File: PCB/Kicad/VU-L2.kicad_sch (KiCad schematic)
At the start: 32 parts, among them U3 SR1-L2, U4 SR2-L2

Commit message: PDF
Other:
- note added: "VU LINE 2"
- moved on the sheet: D31, D32, D33, D34, D35, D36, D37, D38, D39, D40, D41, D42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

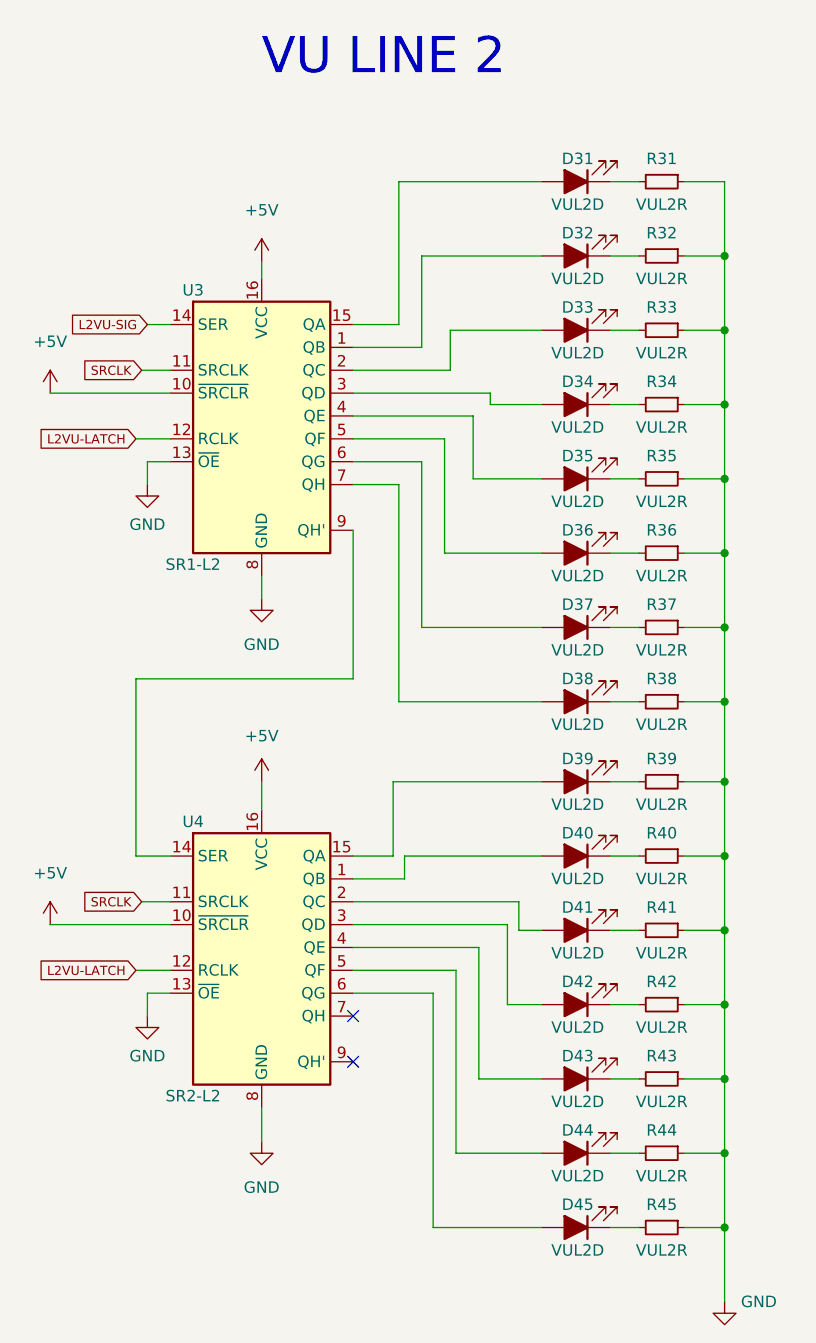
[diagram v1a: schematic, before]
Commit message: added transistor and 3x leds play- cue
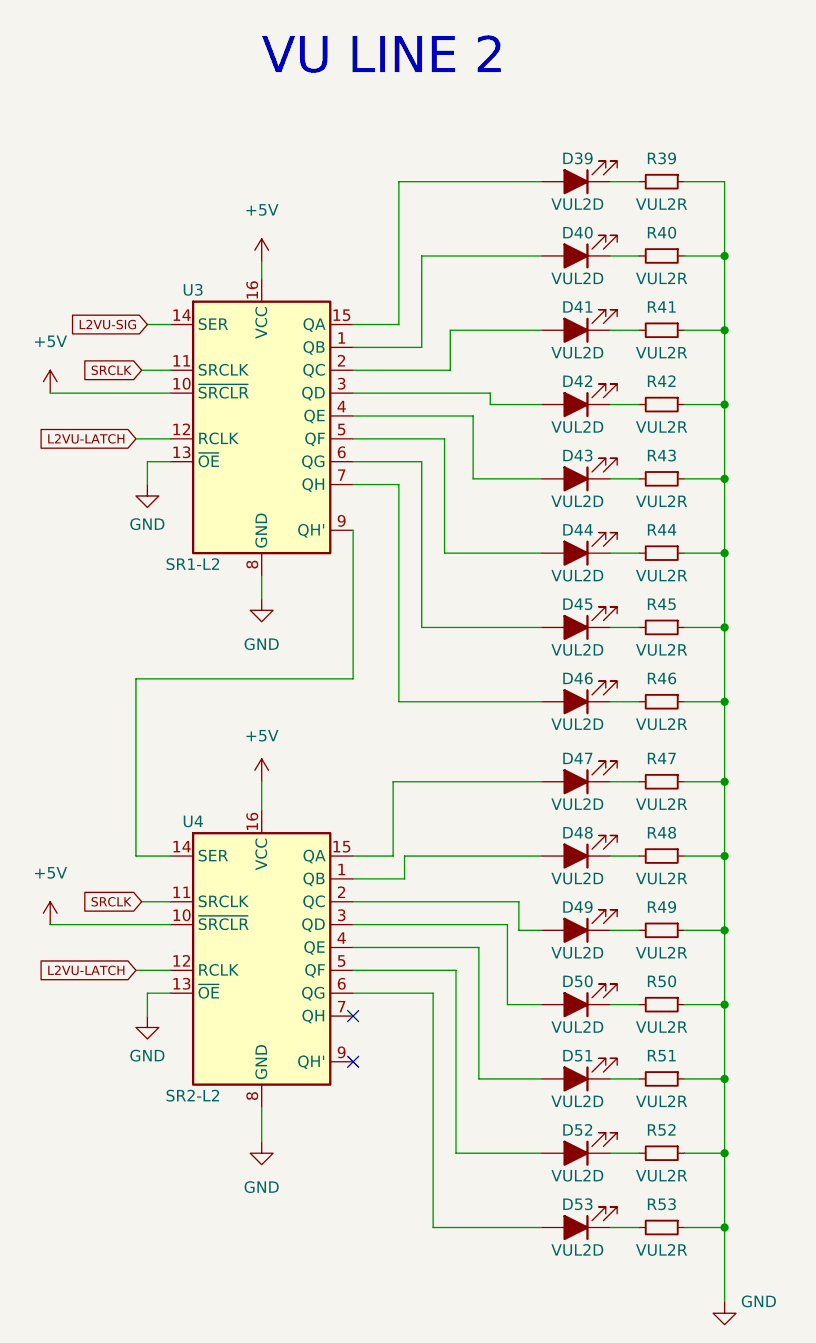
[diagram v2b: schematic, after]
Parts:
- U3, U4: footprint (none) -> Library:SO-16_3.9x9.9mm_P1.27mm
- renumbered D31 to D39, D32 to D40, D33 to D41, D34 to D42, D35 to D43, D36 to D44, D37 to D45, D38 to D46, D39 to D47, D40 to D48, D41 to D49, D42 to D50, D43 to D51, D44 to D52, D45 to D53, R31 to R39, R32 to R40, R33 to R41, R34 to R42, R35 to R43, R36 to R44, R37 to R45, R38 to R46, R39 to R47, R40 to R48, R41 to R49, R42 to R50, R43 to R51, R44 to R52, R45 to R53

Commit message: routing WIP
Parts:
- D48, D49, D50, D51: footprint Library:LED_GREEN -> Library:LED_YELLOW
- D52, D53: footprint Library:LED_GREEN -> Library:LED_RED
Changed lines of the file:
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@@
     (property "Reference" "D48" (id 0) (at 124.6505 120.65 0))
     (property "Value" "VUL2D" (id 1) (at 124.6505 125.73 0))
-    (property "Footprint" "Library:LED_GREEN" (id 2) (at 124.46 123.19 0)
+    (property "Footprint" "Library:LED_YELLOW" (id 2) (at 124.46 123.19 0)
       (effects (font (size 1.27 1.27)) hide)
     )
@@
     (property "Reference" "D49" (id 0) (at 124.6505 128.905 0))
     (property "Value" "VUL2D" (id 1) (at 124.6505 133.985 0))
-    (property "Footprint" "Library:LED_GREEN" (id 2) (at 124.46 131.445 0)
+    (property "Footprint" "Library:LED_YELLOW" (id 2) (at 124.46 131.445 0)
       (effects (font (size 1.27 1.27)) hide)
     )
@@
     (property "Reference" "D50" (id 0) (at 124.6505 137.16 0))
     (property "Value" "VUL2D" (id 1) (at 124.6505 142.24 0))
-    (property "Footprint" "Library:LED_GREEN" (id 2) (at 124.46 139.7 0)
+    (property "Footprint" "Library:LED_YELLOW" (id 2) (at 124.46 139.7 0)
       (effects (font (size 1.27 1.27)) hide)
     )
@@
     (property "Reference" "D51" (id 0) (at 124.6505 145.415 0))
     (property "Value" "VUL2D" (id 1) (at 124.6505 150.495 0))
-    (property "Footprint" "Library:LED_GREEN" (id 2) (at 124.46 147.955 0)
+    (property "Footprint" "Library:LED_YELLOW" (id 2) (at 124.46 147.955 0)
       (effects (font (size 1.27 1.27)) hide)
     )
@@
     (property "Reference" "D52" (id 0) (at 124.6505 153.67 0))
     (property "Value" "VUL2D" (id 1) (at 124.6505 158.75 0))
-    (property "Footprint" "Library:LED_GREEN" (id 2) (at 124.46 156.21 0)
+    (property "Footprint" "Library:LED_RED" (id 2) (at 124.46 156.21 0)
       (effects (font (size 1.27 1.27)) hide)
     )
@@
     (property "Reference" "D53" (id 0) (at 124.6505 161.925 0))
     (property "Value" "VUL2D" (id 1) (at 124.6505 167.005 0))
-    (property "Footprint" "Library:LED_GREEN" (id 2) (at 124.46 164.465 0)
+    (property "Footprint" "Library:LED_RED" (id 2) (at 124.46 164.465 0)
       (effects (font (size 1.27 1.27)) hide)
     )

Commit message: routes finished
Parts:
- D39, D40: footprint Library:LED_GREEN -> Library:LED_RED
- D41, D42, D43, D44: footprint Library:LED_GREEN -> Library:LED_YELLOW
- D48, D49, D50, D51: footprint Library:LED_YELLOW -> Library:LED_GREEN
- D52, D53: footprint Library:LED_RED -> Library:LED_GREEN
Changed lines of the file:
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@@
-(kicad_sch (version 20210615) (generator eeschema)
+(kicad_sch (version 20210621) (generator eeschema)
   (paper "A4")
   (junction (at 140.97 56.515) (diameter 0.9144) (color 0 0 0 0))
@@
     (property "Reference" "D39" (id 0) (at 124.6505 45.72 0))
     (property "Value" "VUL2D" (id 1) (at 124.6505 50.8 0))
-    (property "Footprint" "Library:LED_GREEN" (id 2) (at 124.46 48.26 0)
+    (property "Footprint" "Library:LED_RED" (id 2) (at 124.46 48.26 0)
       (effects (font (size 1.27 1.27)) hide)
     )
@@
     (property "Reference" "D40" (id 0) (at 124.6505 53.975 0))
     (property "Value" "VUL2D" (id 1) (at 124.6505 59.055 0))
-    (property "Footprint" "Library:LED_GREEN" (id 2) (at 124.46 56.515 0)
+    (property "Footprint" "Library:LED_RED" (id 2) (at 124.46 56.515 0)
       (effects (font (size 1.27 1.27)) hide)
     )
@@
     (property "Reference" "D41" (id 0) (at 124.6505 62.23 0))
     (property "Value" "VUL2D" (id 1) (at 124.6505 67.31 0))
-    (property "Footprint" "Library:LED_GREEN" (id 2) (at 124.46 64.77 0)
+    (property "Footprint" "Library:LED_YELLOW" (id 2) (at 124.46 64.77 0)
       (effects (font (size 1.27 1.27)) hide)
     )
@@
     (property "Reference" "D42" (id 0) (at 124.6505 70.485 0))
     (property "Value" "VUL2D" (id 1) (at 124.6505 75.565 0))
-    (property "Footprint" "Library:LED_GREEN" (id 2) (at 124.46 73.025 0)
+    (property "Footprint" "Library:LED_YELLOW" (id 2) (at 124.46 73.025 0)
       (effects (font (size 1.27 1.27)) hide)
     )
@@
     (property "Reference" "D43" (id 0) (at 124.6505 78.74 0))
     (property "Value" "VUL2D" (id 1) (at 124.6505 83.82 0))
-    (property "Footprint" "Library:LED_GREEN" (id 2) (at 124.46 81.28 0)
+    (property "Footprint" "Library:LED_YELLOW" (id 2) (at 124.46 81.28 0)
       (effects (font (size 1.27 1.27)) hide)
     )
@@
     (property "Reference" "D44" (id 0) (at 124.6505 86.995 0))
     (property "Value" "VUL2D" (id 1) (at 124.6505 92.075 0))
-    (property "Footprint" "Library:LED_GREEN" (id 2) (at 124.46 89.535 0)
+    (property "Footprint" "Library:LED_YELLOW" (id 2) (at 124.46 89.535 0)
       (effects (font (size 1.27 1.27)) hide)
     )
@@
     (property "Reference" "D48" (id 0) (at 124.6505 120.65 0))
     (property "Value" "VUL2D" (id 1) (at 124.6505 125.73 0))
-    (property "Footprint" "Library:LED_YELLOW" (id 2) (at 124.46 123.19 0)
+    (property "Footprint" "Library:LED_GREEN" (id 2) (at 124.46 123.19 0)
       (effects (font (size 1.27 1.27)) hide)
     )
@@
     (property "Reference" "D49" (id 0) (at 124.6505 128.905 0))
     (property "Value" "VUL2D" (id 1) (at 124.6505 133.985 0))
-    (property "Footprint" "Library:LED_YELLOW" (id 2) (at 124.46 131.445 0)
+    (property "Footprint" "Library:LED_GREEN" (id 2) (at 124.46 131.445 0)
       (effects (font (size 1.27 1.27)) hide)
     )
@@
     (property "Reference" "D50" (id 0) (at 124.6505 137.16 0))
     (property "Value" "VUL2D" (id 1) (at 124.6505 142.24 0))
-    (property "Footprint" "Library:LED_YELLOW" (id 2) (at 124.46 139.7 0)
+    (property "Footprint" "Library:LED_GREEN" (id 2) (at 124.46 139.7 0)
       (effects (font (size 1.27 1.27)) hide)
     )
@@
     (property "Reference" "D51" (id 0) (at 124.6505 145.415 0))
     (property "Value" "VUL2D" (id 1) (at 124.6505 150.495 0))
-    (property "Footprint" "Library:LED_YELLOW" (id 2) (at 124.46 147.955 0)
+    (property "Footprint" "Library:LED_GREEN" (id 2) (at 124.46 147.955 0)
       (effects (font (size 1.27 1.27)) hide)
     )
@@
     (property "Reference" "D52" (id 0) (at 124.6505 153.67 0))
     (property "Value" "VUL2D" (id 1) (at 124.6505 158.75 0))
-    (property "Footprint" "Library:LED_RED" (id 2) (at 124.46 156.21 0)
+    (property "Footprint" "Library:LED_GREEN" (id 2) (at 124.46 156.21 0)
       (effects (font (size 1.27 1.27)) hide)
     )
@@
     (property "Reference" "D53" (id 0) (at 124.6505 161.925 0))
     (property "Value" "VUL2D" (id 1) (at 124.6505 167.005 0))
-    (property "Footprint" "Library:LED_RED" (id 2) (at 124.46 164.465 0)
-      (effects (font (size 1.27 1.27)) hide)
-    )
+    (property "Footprint" "Library:LED_GREEN" (id 2) (at 124.46 164.465 0)
+      (effects (font (size 1.27 1.27)) hide)
+    )

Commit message: update schematic
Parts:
- R39, R40, R41, R42, R43, R44, R45, R46, R47, R48, R49, R50, R51, R52, R53: footprint Library:R_1206_3216Metric_Pad1.30x1.75mm_HandSolder -> Resistor_SMD:R_1206_3216Metric_Pad1.30x1.75mm_HandSolder
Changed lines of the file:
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@@
     (property "Reference" "R39" (id 0) (at 133.985 45.72 90))
     (property "Value" "VUL2R" (id 1) (at 133.985 50.8 90))
-    (property "Footprint" "Library:R_1206_3216Metric_Pad1.30x1.75mm_HandSolder" (id 2) (at 133.985 48.26 0)
+    (property "Footprint" "Resistor_SMD:R_1206_3216Metric_Pad1.30x1.75mm_HandSolder" (id 2) (at 133.985 48.26 0)
       (effects (font (size 1.27 1.27)) hide)
     )
@@
     (property "Reference" "R40" (id 0) (at 133.985 53.975 90))
     (property "Value" "VUL2R" (id 1) (at 133.985 59.055 90))
-    (property "Footprint" "Library:R_1206_3216Metric_Pad1.30x1.75mm_HandSolder" (id 2) (at 133.985 56.515 0)
+    (property "Footprint" "Resistor_SMD:R_1206_3216Metric_Pad1.30x1.75mm_HandSolder" (id 2) (at 133.985 56.515 0)
       (effects (font (size 1.27 1.27)) hide)
     )
@@
     (property "Reference" "R41" (id 0) (at 133.985 62.23 90))
     (property "Value" "VUL2R" (id 1) (at 133.985 67.31 90))
-    (property "Footprint" "Library:R_1206_3216Metric_Pad1.30x1.75mm_HandSolder" (id 2) (at 133.985 64.77 0)
+    (property "Footprint" "Resistor_SMD:R_1206_3216Metric_Pad1.30x1.75mm_HandSolder" (id 2) (at 133.985 64.77 0)
       (effects (font (size 1.27 1.27)) hide)
     )
@@
     (property "Reference" "R42" (id 0) (at 133.985 70.485 90))
     (property "Value" "VUL2R" (id 1) (at 133.985 75.565 90))
-    (property "Footprint" "Library:R_1206_3216Metric_Pad1.30x1.75mm_HandSolder" (id 2) (at 133.985 73.025 0)
+    (property "Footprint" "Resistor_SMD:R_1206_3216Metric_Pad1.30x1.75mm_HandSolder" (id 2) (at 133.985 73.025 0)
       (effects (font (size 1.27 1.27)) hide)
     )
@@
     (property "Reference" "R43" (id 0) (at 133.985 78.74 90))
     (property "Value" "VUL2R" (id 1) (at 133.985 83.82 90))
-    (property "Footprint" "Library:R_1206_3216Metric_Pad1.30x1.75mm_HandSolder" (id 2) (at 133.985 81.28 0)
+    (property "Footprint" "Resistor_SMD:R_1206_3216Metric_Pad1.30x1.75mm_HandSolder" (id 2) (at 133.985 81.28 0)
       (effects (font (size 1.27 1.27)) hide)
     )
@@
     (property "Reference" "R44" (id 0) (at 133.985 86.995 90))
     (property "Value" "VUL2R" (id 1) (at 133.985 92.075 90))
-    (property "Footprint" "Library:R_1206_3216Metric_Pad1.30x1.75mm_HandSolder" (id 2) (at 133.985 89.535 0)
+    (property "Footprint" "Resistor_SMD:R_1206_3216Metric_Pad1.30x1.75mm_HandSolder" (id 2) (at 133.985 89.535 0)
       (effects (font (size 1.27 1.27)) hide)
     )
@@
     (property "Reference" "R45" (id 0) (at 133.985 95.25 90))
     (property "Value" "VUL2R" (id 1) (at 133.985 100.33 90))
-    (property "Footprint" "Library:R_1206_3216Metric_Pad1.30x1.75mm_HandSolder" (id 2) (at 133.985 97.79 0)
+    (property "Footprint" "Resistor_SMD:R_1206_3216Metric_Pad1.30x1.75mm_HandSolder" (id 2) (at 133.985 97.79 0)
       (effects (font (size 1.27 1.27)) hide)
     )
@@
     (property "Reference" "R46" (id 0) (at 133.985 103.505 90))
     (property "Value" "VUL2R" (id 1) (at 133.985 108.585 90))
-    (property "Footprint" "Library:R_1206_3216Metric_Pad1.30x1.75mm_HandSolder" (id 2) (at 133.985 106.045 0)
+    (property "Footprint" "Resistor_SMD:R_1206_3216Metric_Pad1.30x1.75mm_HandSolder" (id 2) (at 133.985 106.045 0)
       (effects (font (size 1.27 1.27)) hide)
     )
@@
     (property "Reference" "R47" (id 0) (at 133.985 112.395 90))
     (property "Value" "VUL2R" (id 1) (at 133.985 117.475 90))
-    (property "Footprint" "Library:R_1206_3216Metric_Pad1.30x1.75mm_HandSolder" (id 2) (at 133.985 114.935 0)
+    (property "Footprint" "Resistor_SMD:R_1206_3216Metric_Pad1.30x1.75mm_HandSolder" (id 2) (at 133.985 114.935 0)
       (effects (font (size 1.27 1.27)) hide)
     )
@@
     (property "Reference" "R48" (id 0) (at 133.985 120.65 90))
     (property "Value" "VUL2R" (id 1) (at 133.985 125.73 90))
-    (property "Footprint" "Library:R_1206_3216Metric_Pad1.30x1.75mm_HandSolder" (id 2) (at 133.985 123.19 0)
+    (property "Footprint" "Resistor_SMD:R_1206_3216Metric_Pad1.30x1.75mm_HandSolder" (id 2) (at 133.985 123.19 0)
       (effects (font (size 1.27 1.27)) hide)
     )
@@
     (property "Reference" "R49" (id 0) (at 133.985 128.905 90))
     (property "Value" "VUL2R" (id 1) (at 133.985 133.985 90))
-    (property "Footprint" "Library:R_1206_3216Metric_Pad1.30x1.75mm_HandSolder" (id 2) (at 133.985 131.445 0)
+    (property "Footprint" "Resistor_SMD:R_1206_3216Metric_Pad1.30x1.75mm_HandSolder" (id 2) (at 133.985 131.445 0)
       (effects (font (size 1.27 1.27)) hide)
     )
@@
     (property "Reference" "R50" (id 0) (at 133.985 137.16 90))
     (property "Value" "VUL2R" (id 1) (at 133.985 142.24 90))
-    (property "Footprint" "Library:R_1206_3216Metric_Pad1.30x1.75mm_HandSolder" (id 2) (at 133.985 139.7 0)
+    (property "Footprint" "Resistor_SMD:R_1206_3216Metric_Pad1.30x1.75mm_HandSolder" (id 2) (at 133.985 139.7 0)
       (effects (font (size 1.27 1.27)) hide)
     )
@@
     (property "Reference" "R51" (id 0) (at 133.985 145.415 90))
     (property "Value" "VUL2R" (id 1) (at 133.985 150.495 90))
-    (property "Footprint" "Library:R_1206_3216Metric_Pad1.30x1.75mm_HandSolder" (id 2) (at 133.985 147.955 0)
+    (property "Footprint" "Resistor_SMD:R_1206_3216Metric_Pad1.30x1.75mm_HandSolder" (id 2) (at 133.985 147.955 0)
       (effects (font (size 1.27 1.27)) hide)
     )
@@
     (property "Reference" "R52" (id 0) (at 133.985 153.67 90))
     (property "Value" "VUL2R" (id 1) (at 133.985 158.75 90))
-    (property "Footprint" "Library:R_1206_3216Metric_Pad1.30x1.75mm_HandSolder" (id 2) (at 133.985 156.21 0)
+    (property "Footprint" "Resistor_SMD:R_1206_3216Metric_Pad1.30x1.75mm_HandSolder" (id 2) (at 133.985 156.21 0)
       (effects (font (size 1.27 1.27)) hide)
     )
@@
     (property "Reference" "R53" (id 0) (at 133.985 161.925 90))
     (property "Value" "VUL2R" (id 1) (at 133.985 167.005 90))
-    (property "Footprint" "Library:R_1206_3216Metric_Pad1.30x1.75mm_HandSolder" (id 2) (at 133.985 164.465 0)
+    (property "Footprint" "Resistor_SMD:R_1206_3216Metric_Pad1.30x1.75mm_HandSolder" (id 2) (at 133.985 164.465 0)
       (effects (font (size 1.27 1.27)) hide)
     )

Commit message: modified trillbar connectors
Signed-off-by: Jose Vega <josevega234@gmail.com>
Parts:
- U3, U4: footprint Library:SO-16_3.9x9.9mm_P1.27mm -> Package_SO:SOIC-16_3.9x9.9mm_P1.27mm
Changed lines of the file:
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@@
-(kicad_sch (version 20210621) (generator eeschema)
+(kicad_sch (version 20210615) (generator eeschema)
   (paper "A4")
   (junction (at 140.97 56.515) (diameter 0.9144) (color 0 0 0 0))
@@
     (property "Reference" "U3" (id 0) (at 81.915 60.325 0))
     (property "Value" "SR1-L2" (id 1) (at 81.915 90.805 0))
-    (property "Footprint" "Library:SO-16_3.9x9.9mm_P1.27mm" (id 2) (at 89.535 74.295 0)
+    (property "Footprint" "Package_SO:SOIC-16_3.9x9.9mm_P1.27mm" (id 2) (at 89.535 74.295 0)
       (effects (font (size 1.27 1.27)) hide)
     )
@@
     (property "Reference" "U4" (id 0) (at 81.915 119.38 0))
     (property "Value" "SR2-L2" (id 1) (at 81.915 149.86 0))
-    (property "Footprint" "Library:SO-16_3.9x9.9mm_P1.27mm" (id 2) (at 89.535 133.35 0)
-      (effects (font (size 1.27 1.27)) hide)
-    )
+    (property "Footprint" "Package_SO:SOIC-16_3.9x9.9mm_P1.27mm" (id 2) (at 89.535 133.35 0)
+      (effects (font (size 1.27 1.27)) hide)
+    )
